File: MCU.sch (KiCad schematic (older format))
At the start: 10 parts

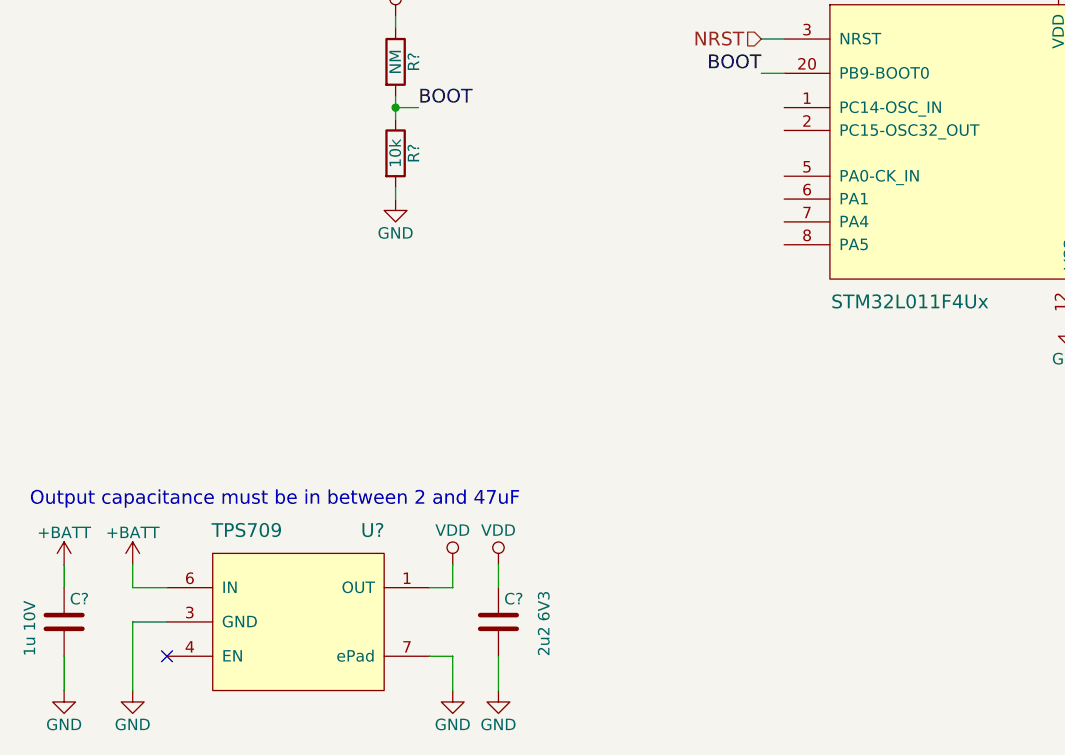
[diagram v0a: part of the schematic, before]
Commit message: Added Hall efect switch
DRV5032
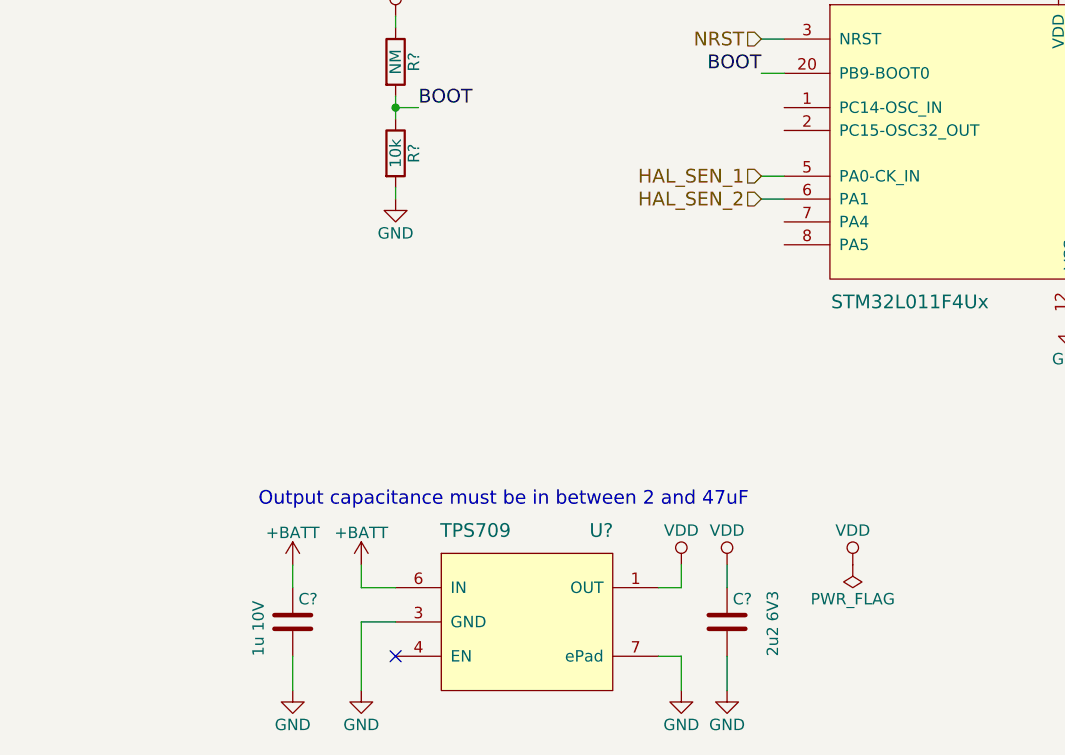
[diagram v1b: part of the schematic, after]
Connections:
- net HAL_SEN_1: now reaches U?.5 (PA0-CK_IN)
- net HAL_SEN_2: now reaches U?.6 (PA1)
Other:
- moved on the sheet: C?, U?
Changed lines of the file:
@@
 LIBS:lakotamm-microprocessors
 LIBS:lakotamm-powersupply
+LIBS:lakotamm-sensor
+LIBS:F3K_Battery_manager-cache
 EELAYER 25 0
 EELAYER END
@@
 L TPS709 U?
 U 1 1 5A9B30C7
-P 2800 6250
-F 0 "U?" H 3100 6650 60  0000 C CNN
-F 1 "TPS709" H 2550 6650 60  0000 C CNN
-F 2 "lakotamm-miscellaneous:WSON-6_2x2mm_Pitch0.65mm" H 2850 5600 60  0001 C CNN
-F 3 "http://www.ti.com/lit/ds/symlink/tps709.pdf" H 2800 5750 60  0001 C CNN
-	1    2800 6250
+P 3800 6250
+F 0 "U?" H 4100 6650 60  0000 C CNN
+F 1 "TPS709" H 3550 6650 60  0000 C CNN
+F 2 "lakotamm-miscellaneous:WSON-6_2x2mm_Pitch0.65mm" H 3850 5600 60  0001 C CNN
+F 3 "http://www.ti.com/lit/ds/symlink/tps709.pdf" H 3800 5750 60  0001 C CNN
+	1    3800 6250
 	1    0    0    -1
 $EndComp
@@
 L GND #PWR?
 U 1 1 5A9B3148
-P 2050 6550
-F 0 "#PWR?" H 2050 6300 50  0001 C CNN
-F 1 "GND" H 2050 6400 50  0000 C CNN
-F 2 "" H 2050 6550 50  0001 C CNN
-F 3 "" H 2050 6550 50  0001 C CNN
-	1    2050 6550
-	1    0    0    -1
-$EndComp
-Wire Wire Line
-	2200 6250 2050 6250
-Wire Wire Line
-	2050 6250 2050 6550
-NoConn ~ 2200 6400
+P 3050 6550
+F 0 "#PWR?" H 3050 6300 50  0001 C CNN
+F 1 "GND" H 3050 6400 50  0000 C CNN
+F 2 "" H 3050 6550 50  0001 C CNN
+F 3 "" H 3050 6550 50  0001 C CNN
+	1    3050 6550
+	1    0    0    -1
+$EndComp
+Wire Wire Line
+	3200 6250 3050 6250
+Wire Wire Line
+	3050 6250 3050 6550
+NoConn ~ 3200 6400
 $Comp
 L GND #PWR?
 U 1 1 5A9B3188
-P 3450 6550
-F 0 "#PWR?" H 3450 6300 50  0001 C CNN
-F 1 "GND" H 3450 6400 50  0000 C CNN
-F 2 "" H 3450 6550 50  0001 C CNN
-F 3 "" H 3450 6550 50  0001 C CNN
-	1    3450 6550
-	1    0    0    -1
-$EndComp
-Wire Wire Line
-	3350 6400 3450 6400
-Wire Wire Line
-	3450 6400 3450 6550
+P 4450 6550
+F 0 "#PWR?" H 4450 6300 50  0001 C CNN
+F 1 "GND" H 4450 6400 50  0000 C CNN
+F 2 "" H 4450 6550 50  0001 C CNN
+F 3 "" H 4450 6550 50  0001 C CNN
+	1    4450 6550
+	1    0    0    -1
+$EndComp
+Wire Wire Line
+	4350 6400 4450 6400
+Wire Wire Line
+	4450 6400 4450 6550
 $Comp
 L VDD #PWR?
 U 1 1 5A9B31B3
-P 3450 6000
-F 0 "#PWR?" H 3450 5850 50  0001 C CNN
-F 1 "VDD" H 3450 6150 50  0000 C CNN
-F 2 "" H 3450 6000 50  0001 C CNN
-F 3 "" H 3450 6000 50  0001 C CNN
-	1    3450 6000
-	1    0    0    -1
-$EndComp
-Wire Wire Line
-	3450 6000 3450 6100
-Wire Wire Line
-	3450 6100 3350 6100
+P 4450 6000
+F 0 "#PWR?" H 4450 5850 50  0001 C CNN
+F 1 "VDD" H 4450 6150 50  0000 C CNN
+F 2 "" H 4450 6000 50  0001 C CNN
+F 3 "" H 4450 6000 50  0001 C CNN
+	1    4450 6000
+	1    0    0    -1
+$EndComp
+Wire Wire Line
+	4450 6000 4450 6100
+Wire Wire Line
+	4450 6100 4350 6100
 $Comp
 L +BATT #PWR?
 U 1 1 5A9B31F8
-P 2050 6000
-F 0 "#PWR?" H 2050 5850 50  0001 C CNN
-F 1 "+BATT" H 2050 6140 50  0000 C CNN
-F 2 "" H 2050 6000 50  0001 C CNN
-F 3 "" H 2050 6000 50  0001 C CNN
-	1    2050 6000
-	1    0    0    -1
-$EndComp
-Wire Wire Line
-	2050 6000 2050 6100
-Wire Wire Line
-	2050 6100 2200 6100
+P 3050 6000
+F 0 "#PWR?" H 3050 5850 50  0001 C CNN
+F 1 "+BATT" H 3050 6140 50  0000 C CNN
+F 2 "" H 3050 6000 50  0001 C CNN
+F 3 "" H 3050 6000 50  0001 C CNN
+	1    3050 6000
+	1    0    0    -1
+$EndComp
+Wire Wire Line
+	3050 6000 3050 6100
+Wire Wire Line
+	3050 6100 3200 6100
 $Comp
 L C C?
 U 1 1 5A9B323D
-P 3650 6250
-F 0 "C?" H 3675 6350 50  0000 L CNN
-F 1 "2u2 6V3" V 3850 6100 50  0000 L CNN
-F 2 "" H 3688 6100 50  0001 C CNN
-F 3 "" H 3650 6250 50  0001 C CNN
-	1    3650 6250
+P 4650 6250
+F 0 "C?" H 4675 6350 50  0000 L CNN
+F 1 "2u2 6V3" V 4850 6100 50  0000 L CNN
+F 2 "" H 4688 6100 50  0001 C CNN
+F 3 "" H 4650 6250 50  0001 C CNN
+	1    4650 6250
 	1    0    0    -1
 $EndComp
@@
 L VDD #PWR?
 U 1 1 5A9B32A8
-P 3650 6000
-F 0 "#PWR?" H 3650 5850 50  0001 C CNN
-F 1 "VDD" H 3650 6150 50  0000 C CNN
-F 2 "" H 3650 6000 50  0001 C CNN
-F 3 "" H 3650 6000 50  0001 C CNN
-	1    3650 6000
+P 4650 6000
+F 0 "#PWR?" H 4650 5850 50  0001 C CNN
+F 1 "VDD" H 4650 6150 50  0000 C CNN
+F 2 "" H 4650 6000 50  0001 C CNN
+F 3 "" H 4650 6000 50  0001 C CNN
+	1    4650 6000
 	1    0    0    -1
 $EndComp
@@
 L GND #PWR?
 U 1 1 5A9B32D5
-P 3650 6550
-F 0 "#PWR?" H 3650 6300 50  0001 C CNN
-F 1 "GND" H 3650 6400 50  0000 C CNN
-F 2 "" H 3650 6550 50  0001 C CNN
-F 3 "" H 3650 6550 50  0001 C CNN
-	1    3650 6550
-	1    0    0    -1
-$EndComp
-Wire Wire Line
-	3650 6000 3650 6100
-Wire Wire Line
-	3650 6400 3650 6550
+P 4650 6550
+F 0 "#PWR?" H 4650 6300 50  0001 C CNN
+F 1 "GND" H 4650 6400 50  0000 C CNN
+F 2 "" H 4650 6550 50  0001 C CNN
+F 3 "" H 4650 6550 50  0001 C CNN
+	1    4650 6550
+	1    0    0    -1
+$EndComp
+Wire Wire Line
+	4650 6000 4650 6100
+Wire Wire Line
+	4650 6400 4650 6550
 $Comp
 L C C?
 U 1 1 5A9B33BC
-P 1750 6250
-F 0 "C?" H 1775 6350 50  0000 L CNN
-F 1 "1u 10V" V 1600 6100 50  0000 L CNN
-F 2 "" H 1788 6100 50  0001 C CNN
-F 3 "" H 1750 6250 50  0001 C CNN
-	1    1750 6250
+P 2750 6250
+F 0 "C?" H 2775 6350 50  0000 L CNN
+F 1 "1u 10V" V 2600 6100 50  0000 L CNN
+F 2 "" H 2788 6100 50  0001 C CNN
+F 3 "" H 2750 6250 50  0001 C CNN
+	1    2750 6250
 	1    0    0    -1
 $EndComp
@@
 L GND #PWR?
 U 1 1 5A9B33C8
-P 1750 6550
-F 0 "#PWR?" H 1750 6300 50  0001 C CNN
-F 1 "GND" H 1750 6400 50  0000 C CNN
-F 2 "" H 1750 6550 50  0001 C CNN
-F 3 "" H 1750 6550 50  0001 C CNN
-	1    1750 6550
-	1    0    0    -1
-$EndComp
-Wire Wire Line
-	1750 6000 1750 6100
-Wire Wire Line
-	1750 6400 1750 6550
+P 2750 6550
+F 0 "#PWR?" H 2750 6300 50  0001 C CNN
+F 1 "GND" H 2750 6400 50  0000 C CNN
+F 2 "" H 2750 6550 50  0001 C CNN
+F 3 "" H 2750 6550 50  0001 C CNN
+	1    2750 6550
+	1    0    0    -1
+$EndComp
+Wire Wire Line
+	2750 6000 2750 6100
+Wire Wire Line
+	2750 6400 2750 6550
 $Comp
 L +BATT #PWR?
 U 1 1 5A9B33E9
-P 1750 6000
-F 0 "#PWR?" H 1750 5850 50  0001 C CNN
-F 1 "+BATT" H 1750 6140 50  0000 C CNN
-F 2 "" H 1750 6000 50  0001 C CNN
-F 3 "" H 1750 6000 50  0001 C CNN
-	1    1750 6000
+P 2750 6000
+F 0 "#PWR?" H 2750 5850 50  0001 C CNN
+F 1 "+BATT" H 2750 6140 50  0000 C CNN
+F 2 "" H 2750 6000 50  0001 C CNN
+F 3 "" H 2750 6000 50  0001 C CNN
+	1    2750 6000
 	1    0    0    -1
 $EndComp
@@
 	1    0    0    -1
 $EndComp
-Text Notes 1600 5750 0    60   ~ 0
+Text Notes 2600 5750 0    60   ~ 0
 Output capacitance must be in between 2 and 47uF\n
 $Comp
@@
 Wire Wire Line
 	7300 4300 7400 4300
+Text HLabel 4800 4300 0    60   Input ~ 0
+HAL_SEN_1
+Wire Wire Line
+	4800 4300 4900 4300
+Text HLabel 4800 4400 0    60   Input ~ 0
+HAL_SEN_2
+Wire Wire Line
+	4800 4400 4900 4400
+$Comp
+L PWR_FLAG #FLG?
+U 1 1 5AA0AD8D
+P 5200 6000
+F 0 "#FLG?" H 5200 6075 50  0001 C CNN
+F 1 "PWR_FLAG" H 5200 6150 50  0000 C CNN
+F 2 "" H 5200 6000 50  0001 C CNN
+F 3 "" H 5200 6000 50  0001 C CNN
+	1    5200 6000
+	-1   0    0    1
+$EndComp
+$Comp
+L VDD #PWR?
+U 1 1 5AA0ADBD
+P 5200 6000
+F 0 "#PWR?" H 5200 5850 50  0001 C CNN
+F 1 "VDD" H 5200 6150 50  0000 C CNN
+F 2 "" H 5200 6000 50  0001 C CNN
+F 3 "" H 5200 6000 50  0001 C CNN
+	1    5200 6000
+	1    0    0    -1
+$EndComp
 $EndSCHEMATC

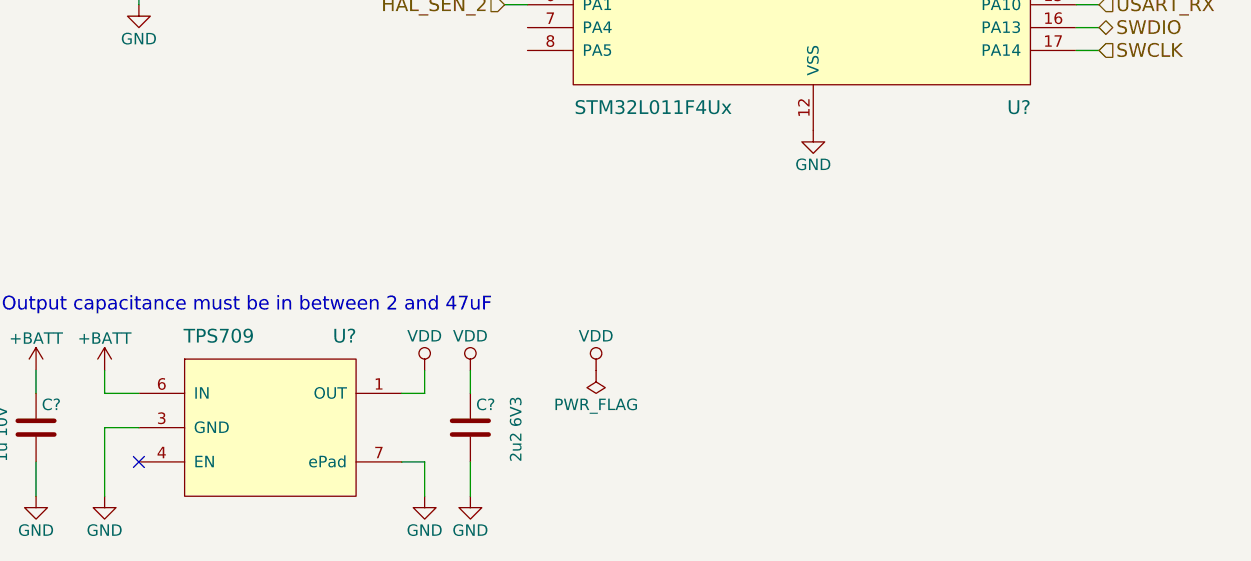
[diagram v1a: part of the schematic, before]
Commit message: Added Buzzer
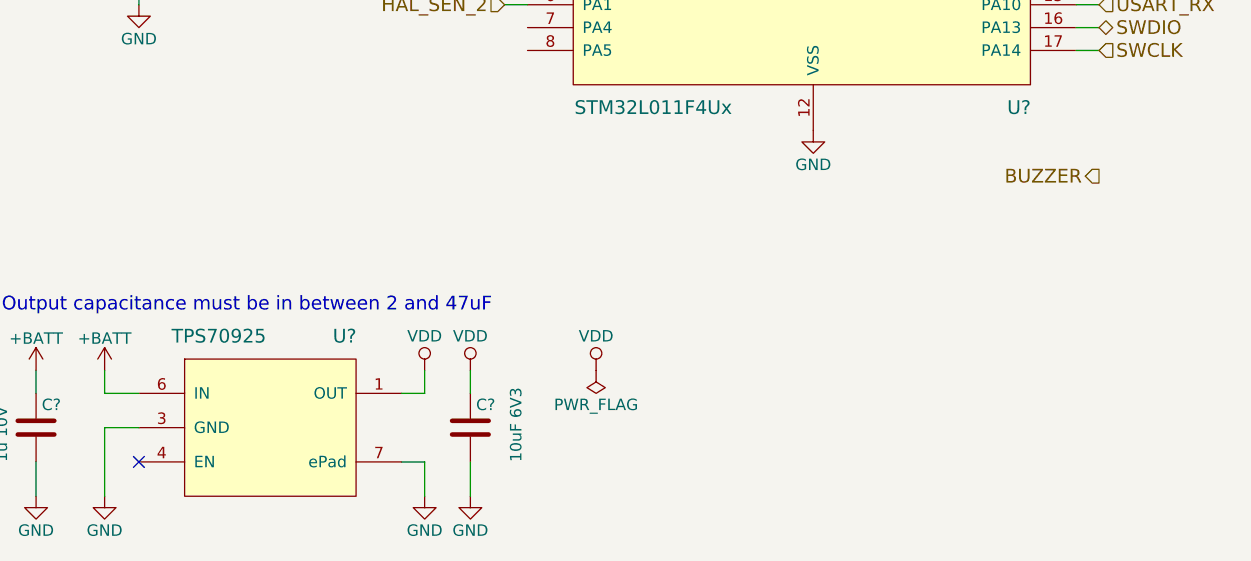
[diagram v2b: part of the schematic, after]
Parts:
- C?: value 2u2 6V3 -> 10uF 6V3
- U?: value TPS709 -> TPS70925
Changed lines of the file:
@@
 LIBS:lakotamm-powersupply
 LIBS:lakotamm-sensor
+LIBS:lakotamm-transistor
 LIBS:F3K_Battery_manager-cache
 EELAYER 25 0
@@
 P 3800 6250
 F 0 "U?" H 4100 6650 60  0000 C CNN
-F 1 "TPS709" H 3550 6650 60  0000 C CNN
+F 1 "TPS70925" H 3550 6650 60  0000 C CNN
 F 2 "lakotamm-miscellaneous:WSON-6_2x2mm_Pitch0.65mm" H 3850 5600 60  0001 C CNN
 F 3 "http://www.ti.com/lit/ds/symlink/tps709.pdf" H 3800 5750 60  0001 C CNN
@@
 P 4650 6250
 F 0 "C?" H 4675 6350 50  0000 L CNN
-F 1 "2u2 6V3" V 4850 6100 50  0000 L CNN
+F 1 "10uF 6V3" V 4850 6100 50  0000 L CNN
 F 2 "" H 4688 6100 50  0001 C CNN
 F 3 "" H 4650 6250 50  0001 C CNN
@@
 	1    0    0    -1
 $EndComp
+Text HLabel 7400 5150 0    60   Output ~ 0
+BUZZER
 $EndSCHEMATC
